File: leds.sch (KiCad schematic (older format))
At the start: 218 parts

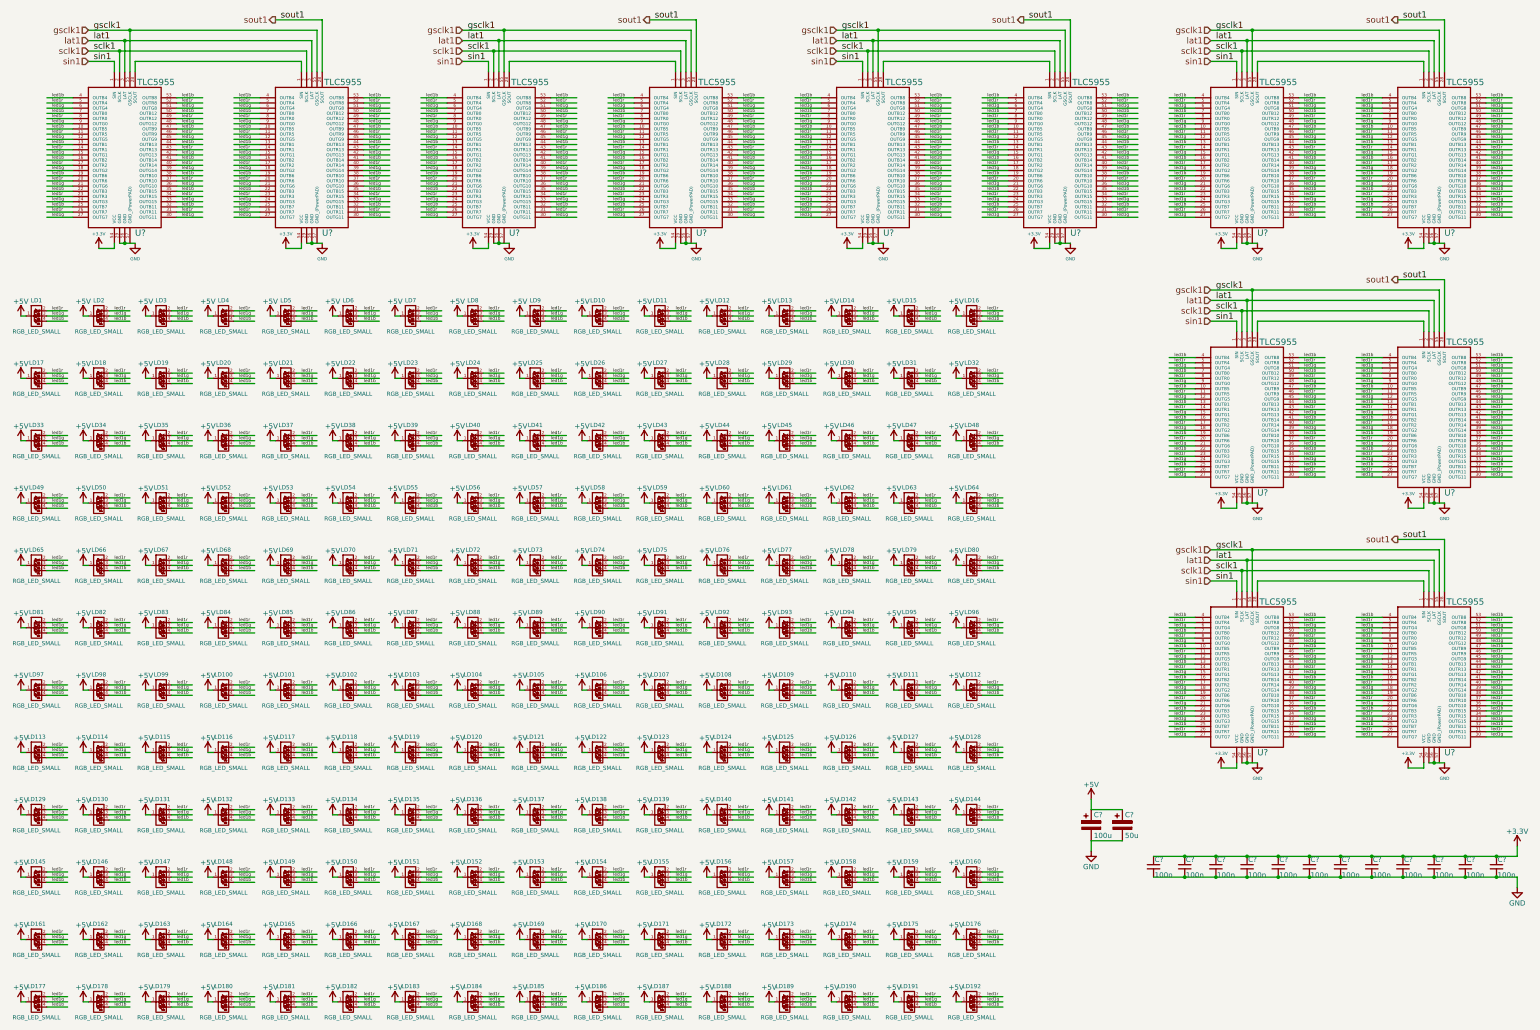
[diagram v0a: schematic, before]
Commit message: Fix sin/sclk/sout/lat/gsclk 1-6 pins and labels.
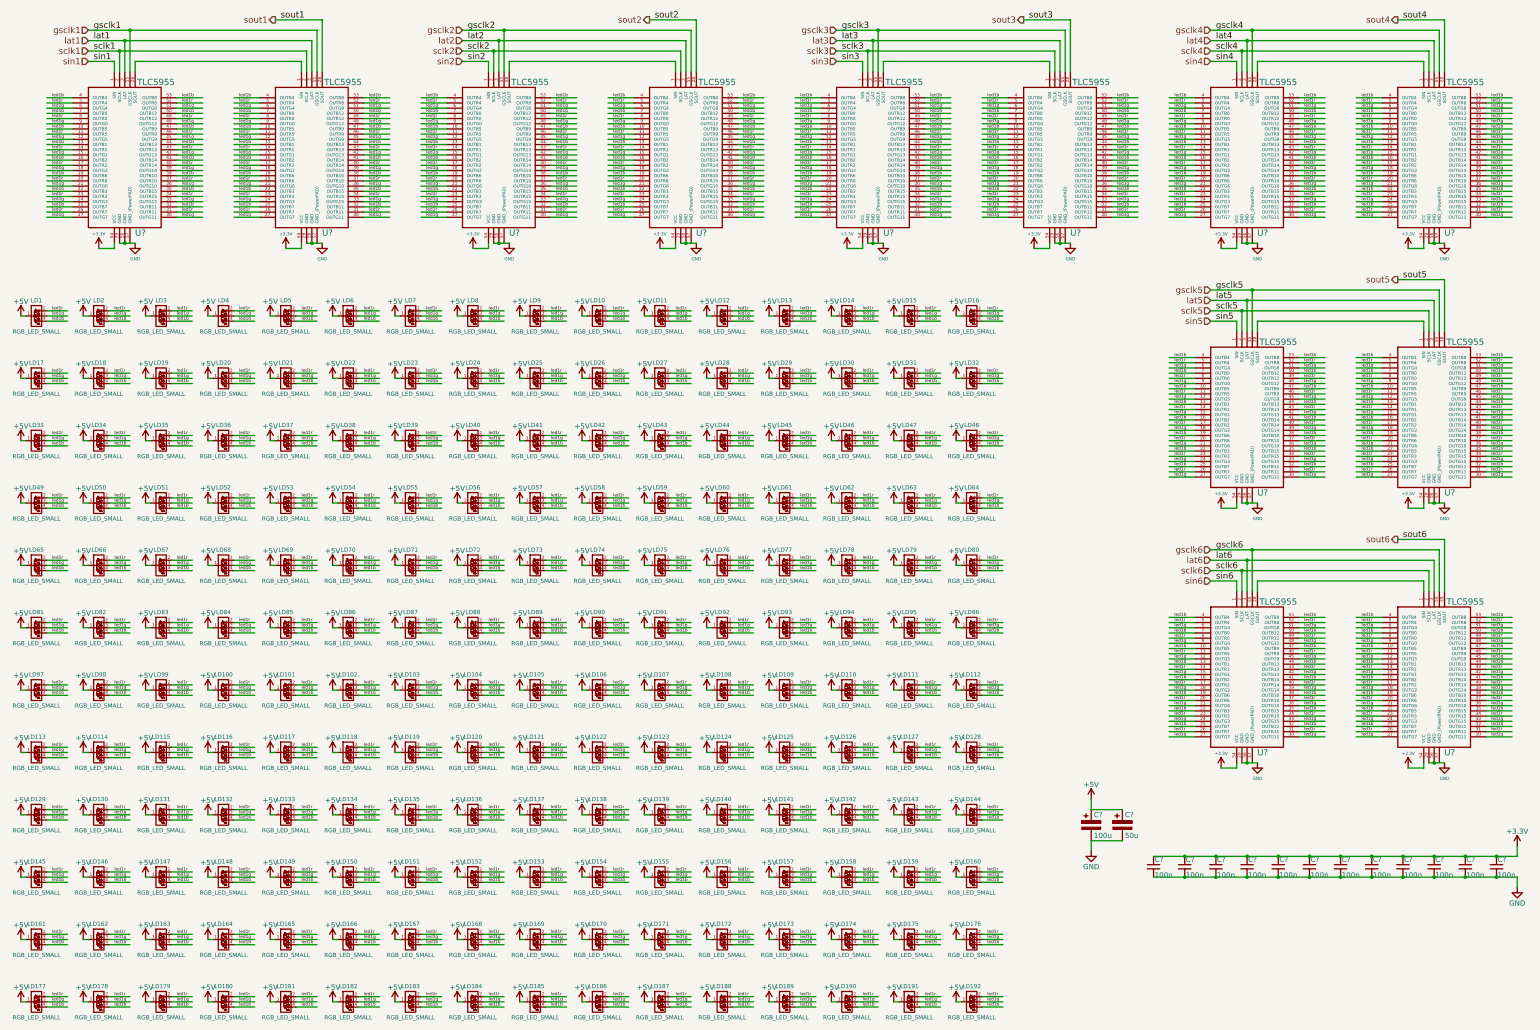
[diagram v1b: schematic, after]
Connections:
- net labels added: gsclk2, gsclk3, gsclk4, gsclk5, gsclk6, lat2, lat3, lat4, lat5, lat6, sclk2, sclk3, sclk4, sclk5, sclk6, sin2, sin3, sin4, sin5, sin6, sout2, sout3, sout4, sout5, sout6
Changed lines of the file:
@@
 	5700 1550 5450 1550
 Text Label 5500 1550 0    60   ~ 0
-sin1
+sin2
 Text Label 5500 1450 0    60   ~ 0
-sclk1
+sclk2
 Text Label 5500 1350 0    60   ~ 0
-lat1
+lat2
 Text Label 5500 1250 0    60   ~ 0
-gsclk1
+gsclk2
 Wire Wire Line
 	5850 1650 5850 1250
@@
 	5750 1450 5750 1650
 Text HLabel 5450 1250 0    60   Input ~ 0
-gsclk1
+gsclk2
 Text HLabel 5450 1350 0    60   Input ~ 0
-lat1
+lat2
 Text HLabel 5450 1450 0    60   Input ~ 0
-sclk1
+sclk2
 Text HLabel 5450 1550 0    60   Input ~ 0
-sin1
+sin2
 $Comp
 L TLC5955 U?
@@
 	5900 1550 7500 1550
 Text Label 7300 1150 0    60   ~ 0
-sout1
+sout2
 Wire Wire Line
 	7250 1150 7700 1150
@@
 	7550 1450 7550 1650
 Text HLabel 7250 1150 0    60   Output ~ 0
-sout1
+sout2
 Wire Wire Line
 	5900 1650 5900 1550
@@
 	9300 1550 9050 1550
 Text Label 9100 1550 0    60   ~ 0
-sin1
+sin3
 Text Label 9100 1450 0    60   ~ 0
-sclk1
+sclk3
 Text Label 9100 1350 0    60   ~ 0
-lat1
+lat3
 Text Label 9100 1250 0    60   ~ 0
-gsclk1
+gsclk3
 Wire Wire Line
 	9450 1650 9450 1250
@@
 	9350 1450 9350 1650
 Text HLabel 9050 1250 0    60   Input ~ 0
-gsclk1
+gsclk3
 Text HLabel 9050 1350 0    60   Input ~ 0
-lat1
+lat3
 Text HLabel 9050 1450 0    60   Input ~ 0
-sclk1
+sclk3
 Text HLabel 9050 1550 0    60   Input ~ 0
-sin1
+sin3
 $Comp
 L TLC5955 U?
@@
 	9500 1550 11100 1550
 Text Label 10900 1150 0    60   ~ 0
-sout1
+sout3
 Wire Wire Line
 	10850 1150 11300 1150
@@
 	11150 1450 11150 1650
 Text HLabel 10850 1150 0    60   Output ~ 0
-sout1
+sout3
 Wire Wire Line
 	9500 1650 9500 1550
@@
 	12900 1550 12650 1550
 Text Label 12700 1550 0    60   ~ 0
-sin1
+sin4
 Text Label 12700 1450 0    60   ~ 0
-sclk1
+sclk4
 Text Label 12700 1350 0    60   ~ 0
-lat1
+lat4
 Text Label 12700 1250 0    60   ~ 0
-gsclk1
+gsclk4
 Wire Wire Line
 	13050 1650 13050 1250
@@
 	12950 1450 12950 1650
 Text HLabel 12650 1250 0    60   Input ~ 0
-gsclk1
+gsclk4
 Text HLabel 12650 1350 0    60   Input ~ 0
-lat1
+lat4
 Text HLabel 12650 1450 0    60   Input ~ 0
-sclk1
+sclk4
 Text HLabel 12650 1550 0    60   Input ~ 0
-sin1
+sin4
 $Comp
 L TLC5955 U?
@@
 	13100 1550 14700 1550
 Text Label 14500 1150 0    60   ~ 0
-sout1
+sout4
 Wire Wire Line
 	14450 1150 14900 1150
@@
 	14750 1450 14750 1650
 Text HLabel 14450 1150 0    60   Output ~ 0
-sout1
+sout4
 Wire Wire Line
 	13100 1650 13100 1550
@@
 	12900 4050 12650 4050
 Text Label 12700 4050 0    60   ~ 0
-sin1
+sin5
 Text Label 12700 3950 0    60   ~ 0
-sclk1
+sclk5
 Text Label 12700 3850 0    60   ~ 0
-lat1
+lat5
 Text Label 12700 3750 0    60   ~ 0
-gsclk1
+gsclk5
 Wire Wire Line
 	13050 4150 13050 3750
@@
 	12950 3950 12950 4150
 Text HLabel 12650 3750 0    60   Input ~ 0
-gsclk1
+gsclk5
 Text HLabel 12650 3850 0    60   Input ~ 0
-lat1
+lat5
 Text HLabel 12650 3950 0    60   Input ~ 0
-sclk1
+sclk5
 Text HLabel 12650 4050 0    60   Input ~ 0
-sin1
+sin5
 $Comp
 L TLC5955 U?
@@
 	13100 4050 14700 4050
 Text Label 14500 3650 0    60   ~ 0
-sout1
+sout5
 Wire Wire Line
 	14450 3650 14900 3650
@@
 	14750 3950 14750 4150
 Text HLabel 14450 3650 0    60   Output ~ 0
-sout1
+sout5
 Wire Wire Line
 	13100 4150 13100 4050
@@
 	12900 6550 12650 6550
 Text Label 12700 6550 0    60   ~ 0
-sin1
+sin6
 Text Label 12700 6450 0    60   ~ 0
-sclk1
+sclk6
 Text Label 12700 6350 0    60   ~ 0
-lat1
+lat6
 Text Label 12700 6250 0    60   ~ 0
-gsclk1
+gsclk6
 Wire Wire Line
 	13050 6650 13050 6250
@@
 	12950 6450 12950 6650
 Text HLabel 12650 6250 0    60   Input ~ 0
-gsclk1
+gsclk6
 Text HLabel 12650 6350 0    60   Input ~ 0
-lat1
+lat6
 Text HLabel 12650 6450 0    60   Input ~ 0
-sclk1
+sclk6
 Text HLabel 12650 6550 0    60   Input ~ 0
-sin1
+sin6
 $Comp
 L TLC5955 U?
@@
 	13100 6550 14700 6550
 Text Label 14500 6150 0    60   ~ 0
-sout1
+sout6
 Wire Wire Line
 	14450 6150 14900 6150
@@
 	14750 6450 14750 6650
 Text HLabel 14450 6150 0    60   Output ~ 0
-sout1
+sout6
 Wire Wire Line
 	13100 6650 13100 6550

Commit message: Assign labels led{1..192}{r,g,b} to all LED pins.
(This is just an intermediate assignment to TLC outputs; real
assignments will be determined later, according to what works best for
the PCB routing).
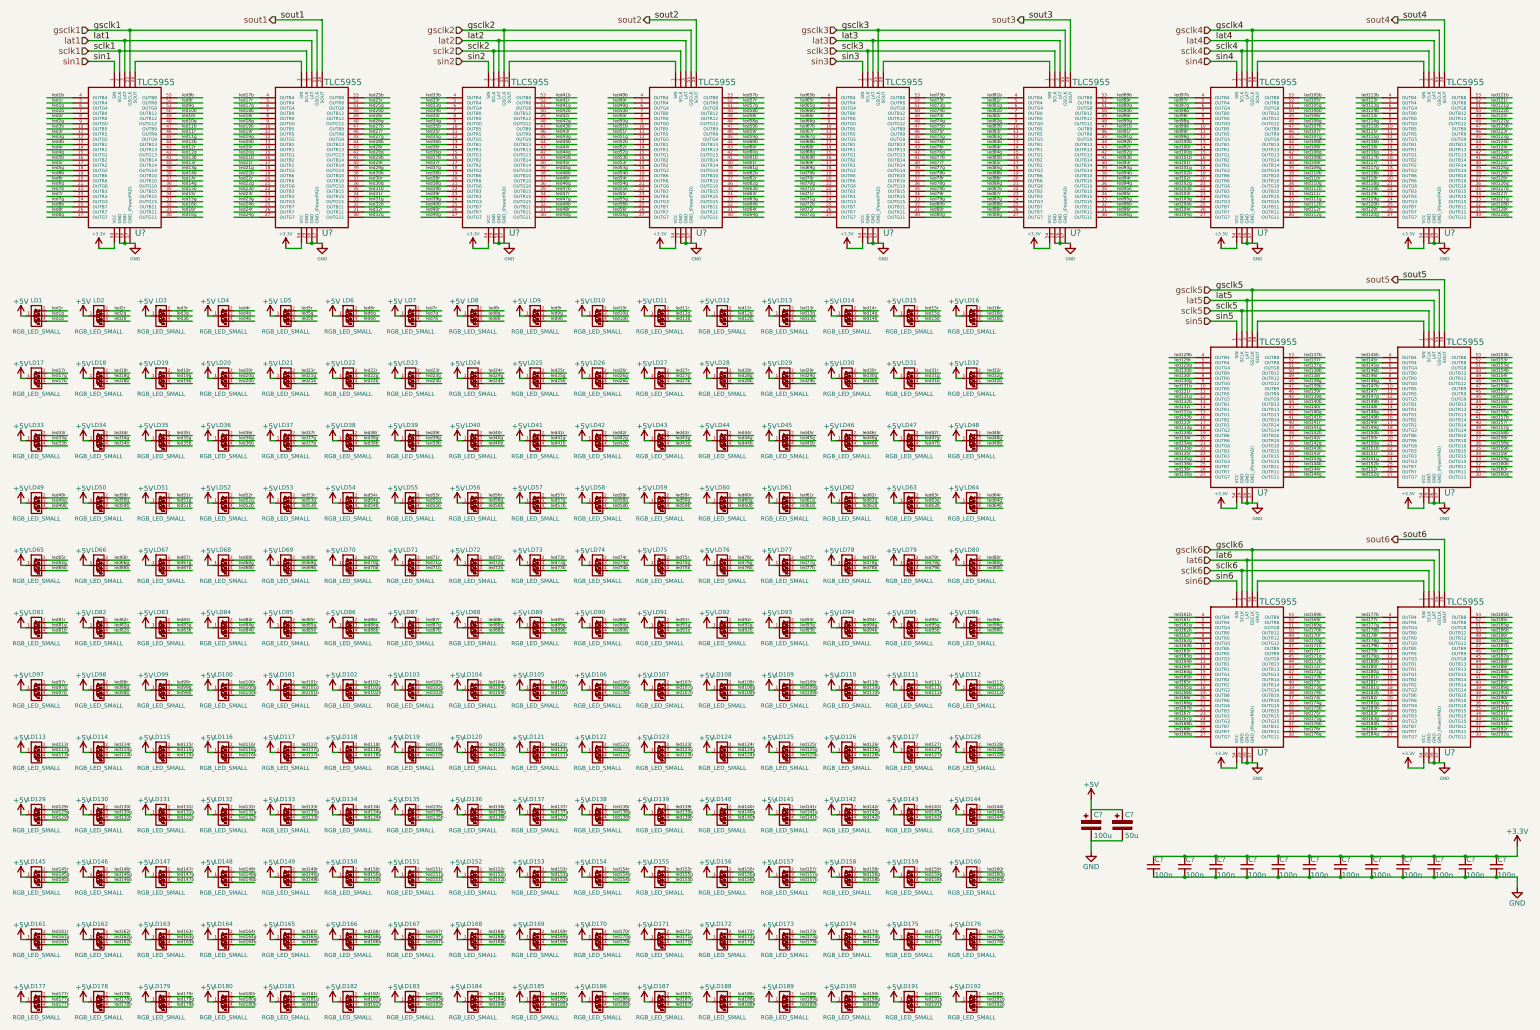
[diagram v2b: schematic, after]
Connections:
- net labels added: led100b, led100g, led100r, led101b, led101g, led101r, led102b, led102g, led102r, led103b, led103g, led103r, led104b, led104g, led104r, led105b, led105g, led105r, led106b, led106g, led106r, led107b, led107g, led107r, led108b, led108g, led108r, led109b, led109g, led109r, led10b, led10g, led10r, led110b, led110g, led110r, led111b, led111g, led111r, led112b, led112g, led112r, led113b, led113g, led113r, led114b, led114g, led114r, led115b, led115g, led115r, led116b, led116g, led116r, led117b, led117g, led117r, led118b, led118g, led118r, led119b, led119g, led119r, led11b, led11g, led11r, led120b, led120g, led120r, led121b, led121g, led121r, led122b, led122g, led122r, led123b, led123g, led123r, led124b, led124g, led124r, led125b, led125g, led125r, led126b, led126g, led126r, led127b, led127g, led127r, led128b, led128g, led128r, led129b, led129g, led129r, led12b, led12g, led12r, led130b, led130g, led130r, led131b, led131g, led131r, led132b, led132g, led132r, led133b, led133g, led133r, led134b, led134g, led134r, led135b, led135g, led135r, led136b, led136g, led136r, led137b, led137g, led137r, led138b, led138g, led138r, led139b, led139g, led139r, led13b, led13g, led13r, led140b, led140g, led140r, led141b, led141g, led141r, led142b, led142g, led142r, led143b, led143g, led143r, led144b, led144g, led144r, led145b, led145g, led145r, led146b, led146g, led146r, led147b, led147g, led147r, led148b, led148g, led148r, led149b, led149g, led149r, led14b, led14g, led14r, led150b, led150g, led150r, led151b, led151g, led151r, led152b, led152g, led152r, led153b, led153g, led153r, led154b, led154g, led154r, led155b, led155g, led155r, led156b, led156g, led156r, led157b, led157g, led157r, led158b, led158g, led158r, led159b, led159g, led159r, led15b, led15g, led15r, led160b, led160g, led160r, led161b, led161g, led161r, led162b, led162g, led162r, led163b, led163g, led163r, led164b, led164g, led164r, led165b, led165g, led165r, led166b, led166g, led166r, led167b, led167g, led167r, led168b, led168g, led168r, led169b, led169g, led169r, led16b, led16g, led16r, led170b, led170g, led170r, led171b, led171g, led171r, led172b, led172g, led172r, led173b, led173g, led173r, led174b, led174g, led174r, led175b, led175g, led175r, led176b, led176g, led176r, led177b, led177g, led177r, led178b, led178g, led178r, led179b, led179g, led179r, led17b, led17g, led17r, led180b, led180g, led180r, led181b, led181g, led181r, led182b, led182g, led182r, led183b, led183g, led183r, led184b, led184g, led184r, led185b, led185g, led185r, led186b, led186g, led186r, led187b, led187g, led187r, led188b, led188g, led188r, led189b, led189g, led189r, led18b, led18g, led18r, led190b, led190g, led190r, led191b, led191g, led191r, led192b, led192g, led192r, led19b, led19g, led19r, led20b, led20g, led20r, led21b, led21g, led21r, led22b, led22g, led22r, led23b, led23g, led23r, led24b, led24g, led24r, led25b, led25g, led25r, led26b, led26g, led26r, led27b, led27g, led27r, led28b, led28g, led28r, led29b, led29g, led29r, led2b, led2g, led2r, led30b, led30g, led30r, led31b, led31g, led31r, led32b, led32g, led32r, led33b, led33g, led33r, led34b, led34g, led34r, led35b, led35g, led35r, led36b, led36g, led36r, led37b, led37g, led37r, led38b, led38g, led38r, led39b, led39g, led39r, led3b, led3g, led3r, led40b, led40g, led40r, led41b, led41g, led41r, led42b, led42g, led42r, led43b, led43g, led43r, led44b, led44g, led44r, led45b, led45g, led45r, led46b, led46g, led46r, led47b, led47g, led47r, led48b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

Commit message: Misc. small fixes, DRC (almost) passes now.
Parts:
- gave numbers to parts that had none: 26

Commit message: Basic netlist with footprint assignment and import into pcbnew
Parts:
- C32, C33: footprint (none) -> w_smd_cap:c_elec_6.3x5.8
- C34, C35, C36, C37, C38, C39, C40, C41, C42, C43, C44, C45: footprint (none) -> w_smd_cap:c_0805
- LD1, LD10, LD100, LD101, LD102, LD103, LD104, LD105, LD106, LD107, LD108, LD109, LD11, LD110, LD111, LD112, LD113, LD114, LD115, LD116, LD117, LD118, LD119, LD12, LD120, LD121, LD122, LD123, LD124, LD125, LD126, LD127, LD128, LD129, LD13, LD130, LD131, LD132, LD133, LD134, LD135, LD136, LD137, LD138, LD139, LD14, LD140, LD141, LD142, LD143, LD144, LD145, LD146, LD147, LD148, LD149, LD15, LD150, LD151, LD152, LD153, LD154, LD155, LD156, LD157, LD158, LD159, LD16, LD160, LD161, LD162, LD163, LD164, LD165, LD166, LD167, LD168, LD169, LD17, LD170, LD171, LD172, LD173, LD174, LD175, LD176, LD177, LD178, LD179, LD18, LD180, LD181, LD182, LD183, LD184, LD185, LD186, LD187, LD188, LD189, LD19, LD190, LD191, LD192, LD2, LD20, LD21, LD22, LD23, LD24, LD25, LD26, LD27, LD28, LD29, LD3, LD30, LD31, LD32, LD33, LD34, LD35, LD36, LD37, LD38, LD39, LD4, LD40, LD41, LD42, LD43, LD44, LD45, LD46, LD47, LD48, LD49, LD5, LD50, LD51, LD52, LD53, LD54, LD55, LD56, LD57, LD58, LD59, LD6, LD60, LD61, LD62, LD63, LD64, LD65, LD66, LD67, LD68, LD69, LD7, LD70, LD71, LD72, LD73, LD74, LD75, LD76, LD77, LD78, LD79, LD8, LD80, LD81, LD82, LD83, LD84, LD85, LD86, LD87, LD88, LD89, LD9, LD90, LD91, LD92, LD93, LD94, LD95, LD96, LD97, LD98, LD99: footprint (none) -> knielsenlib:RGB_0603
- U10, U11, U12, U13, U14, U15, U4, U5, U6, U7, U8, U9: footprint (none) -> knielsenlib:TLC5955DCA

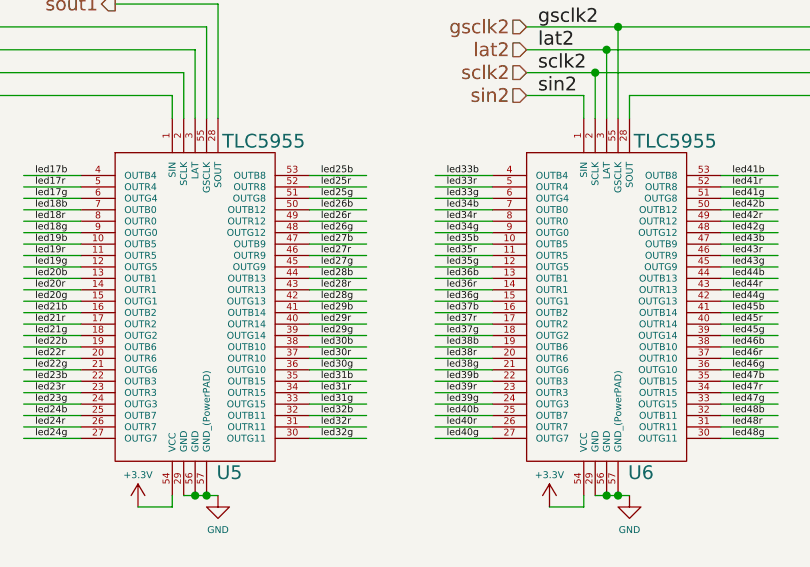
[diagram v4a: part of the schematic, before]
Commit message: Some experiments with a way to route the LEDs
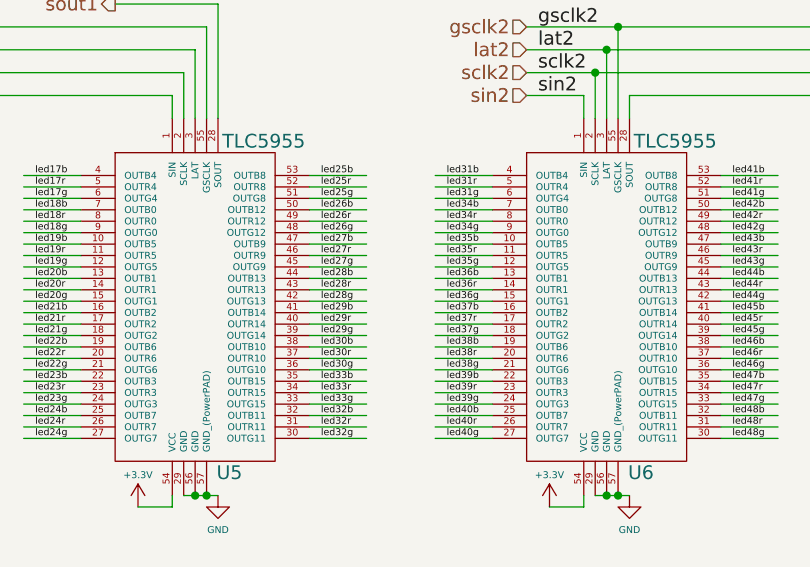
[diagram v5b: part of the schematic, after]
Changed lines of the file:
@@
 	4750 2900 4500 2900
 Text Label 4550 2800 0    30   ~ 0
-led31b
+led33b
 Text Label 4550 2850 0    30   ~ 0
-led31r
+led33r
 Text Label 4550 2900 0    30   ~ 0
-led31g
+led33g
 Wire Wire Line
 	4750 2950 4500 2950
@@
 	5300 2000 5050 2000
 Text Label 5100 1900 0    30   ~ 0
-led33b
+led31b
 Text Label 5100 1950 0    30   ~ 0
-led33r
+led31r
 Text Label 5100 2000 0    30   ~ 0
-led33g
+led31g
 Wire Wire Line
 	5300 2050 5050 2050
